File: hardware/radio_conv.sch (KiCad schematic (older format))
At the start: 15 parts

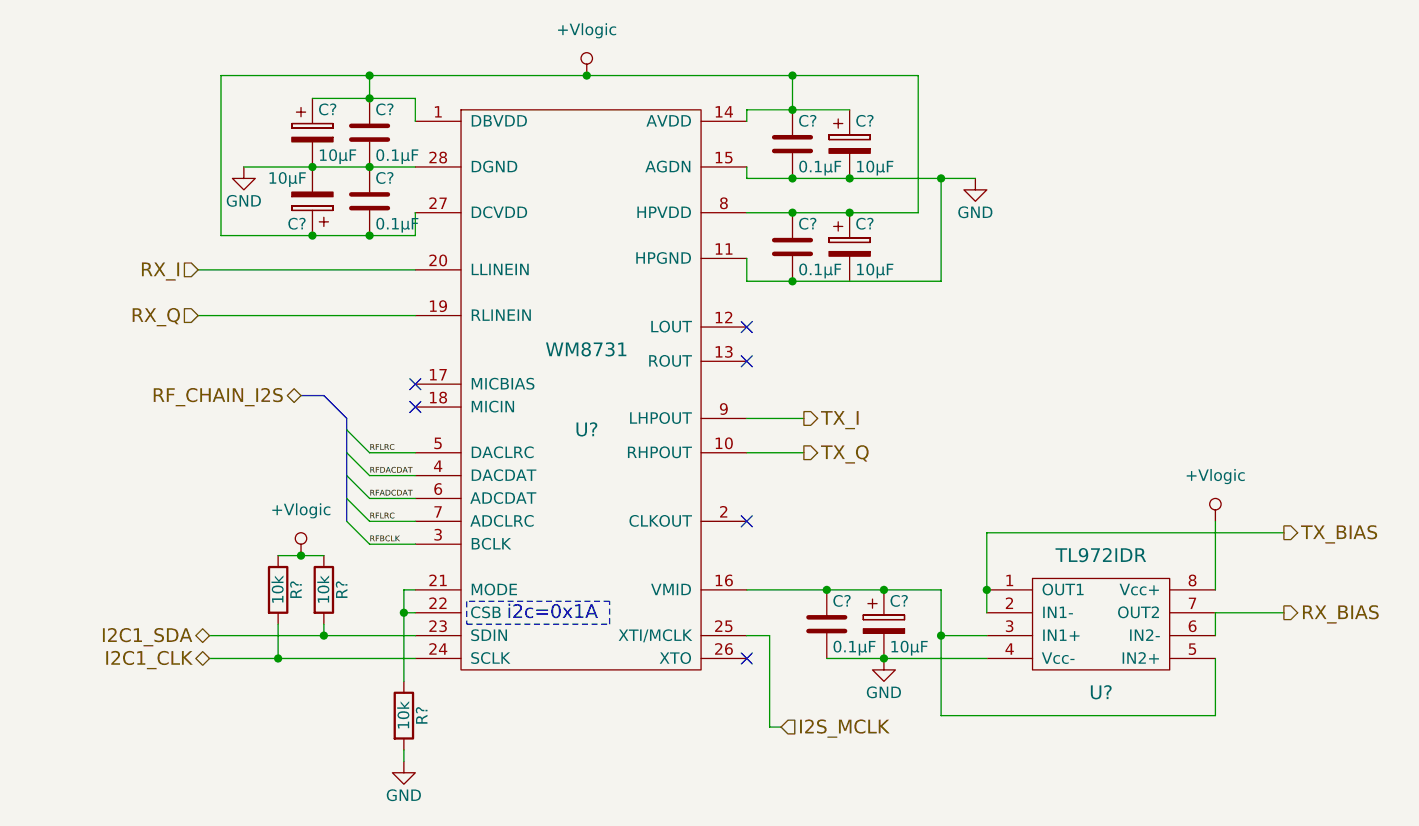
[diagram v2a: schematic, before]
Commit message: Allocated CPU some pins and made minor adjustments here and there
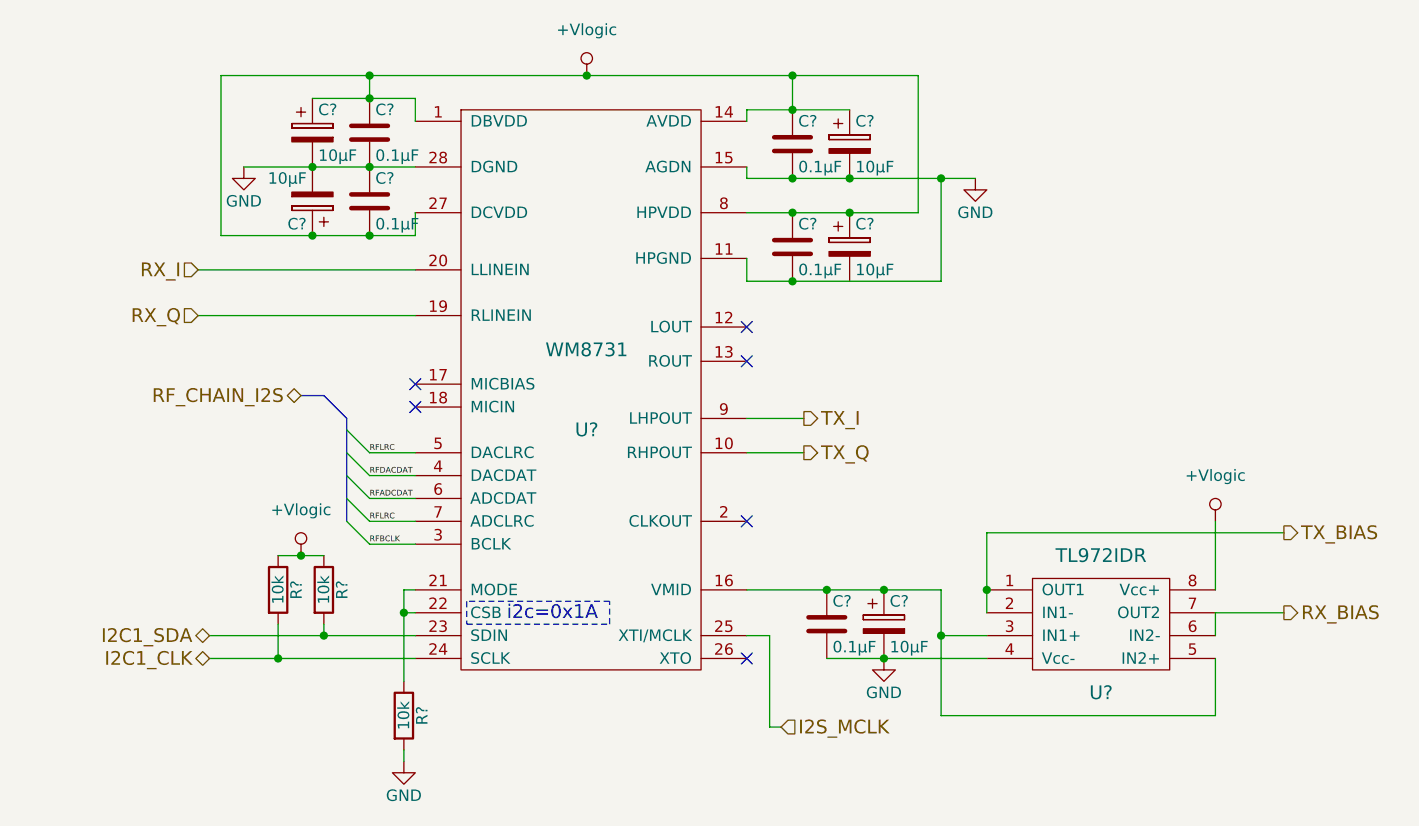
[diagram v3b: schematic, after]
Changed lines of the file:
@@
 $EndComp
 Wire Wire Line
-	4300 2600 4600 2600
-Wire Wire Line
-	4600 2600 4850 2600
-Wire Wire Line
-	4850 2600 5050 2600
+	4300 2600 5050 2600
 Wire Wire Line
 	5050 2300 5050 2400
 Wire Wire Line
-	4600 2300 4850 2300
-Wire Wire Line
-	4850 2300 5050 2300
+	4600 2300 5050 2300
 Connection ~ 4850 2300
 Wire Wire Line
 	4850 2300 4850 2200
 Wire Wire Line
-	4200 2200 4850 2200
-Wire Wire Line
-	4850 2200 5800 2200
-Wire Wire Line
-	5800 2200 6700 2200
-Wire Wire Line
-	6700 2200 7250 2200
+	4200 2200 7250 2200
 Connection ~ 4600 2600
 Connection ~ 4850 2600
@@
 Connection ~ 5800 2200
 Wire Wire Line
-	6500 2350 6700 2350
-Wire Wire Line
-	6700 2350 6950 2350
+	6500 2350 6950 2350
 Wire Wire Line
 	6500 2350 6500 2400
 Connection ~ 6700 2350
 Wire Wire Line
-	6500 2650 6700 2650
-Wire Wire Line
-	6700 2650 6950 2650
-Wire Wire Line
-	6950 2650 7350 2650
-Wire Wire Line
-	7350 2650 7500 2650
+	6500 2650 7500 2650
 Wire Wire Line
 	6500 2650 6500 2600
@@
 	7250 2800 7250 2200
 Wire Wire Line
-	6500 2800 6700 2800
-Wire Wire Line
-	6700 2800 6950 2800
-Wire Wire Line
-	6950 2800 7250 2800
+	6500 2800 7250 2800
 Connection ~ 6700 2200
 Connection ~ 6950 2800
@@
 	6500 3000 6500 3100
 Wire Wire Line
-	6500 3100 6700 3100
-Wire Wire Line
-	6700 3100 7350 3100
+	6500 3100 7350 3100
 Wire Wire Line
 	7350 3100 7350 2650
@@
 NoConn ~ 5050 3650
 Wire Wire Line
-	4200 2900 4600 2900
-Wire Wire Line
-	4600 2900 4850 2900
-Wire Wire Line
-	4850 2900 5050 2900
+	4200 2900 5050 2900
 Wire Wire Line
 	5050 2900 5050 2800
@@
 $EndComp
 Wire Wire Line
-	4150 4650 4650 4650
-Wire Wire Line
-	4650 4650 5050 4650
+	4150 4650 5050 4650
 Wire Wire Line
 	4650 4650 4650 4600
 Wire Wire Line
-	4150 4750 4450 4750
-Wire Wire Line
-	4450 4750 5050 4750
+	4150 4750 5050 4750
 Wire Wire Line
 	4450 4750 4450 4600
@@
 $EndComp
 Wire Wire Line
-	6500 4450 6850 4450
-Wire Wire Line
-	6850 4450 7100 4450
-Wire Wire Line
-	7100 4450 7350 4450
+	6500 4450 7350 4450
 Connection ~ 6850 4450
 Wire Wire Line
-	6850 4750 7100 4750
-Wire Wire Line
-	7100 4750 7550 4750
+	6850 4750 7550 4750
 $Comp
 L GND #PWR043
@@
 	4650 3600 4750 3700
 Wire Bus Line
-	4750 3700 4750 3750
-Wire Bus Line
-	4750 3750 4750 3850
-Wire Bus Line
-	4750 3850 4750 3950
-Wire Bus Line
-	4750 3950 4750 4050
-Wire Bus Line
-	4750 4050 4750 4150
+	4750 3700 4750 4150
 Wire Bus Line
 	4650 3600 4550 3600
@@
 	5050 4550 5000 4550
 Wire Wire Line
-	5000 4450 5000 4550
-Wire Wire Line
-	5000 4550 5000 4850
+	5000 4450 5000 4850
 Text Notes 5450 4590 0    60   ~ 0
 i2c=0x1A
@@
 $EndComp
 Wire Wire Line
-	7350 4450 7350 4650
-Wire Wire Line
-	7350 4650 7350 5000
+	7350 4450 7350 5000
 Wire Wire Line
 	7350 4650 7550 4650
@@
 Connection ~ 7100 4750
 Wire Wire Line
-	7550 4200 7550 4450
-Wire Wire Line
-	7550 4450 7550 4550
+	7550 4200 7550 4550
 Wire Wire Line
 	8550 4550 8550 4650
@@
 Connection ~ 5000 4550
 Wire Wire Line
-	4450 4300 4550 4300
-Wire Wire Line
-	4550 4300 4650 4300
+	4450 4300 4650 4300
 Wire Wire Line
 	5000 4450 5050 4450

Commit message: Fixed 8/11 of issue #4
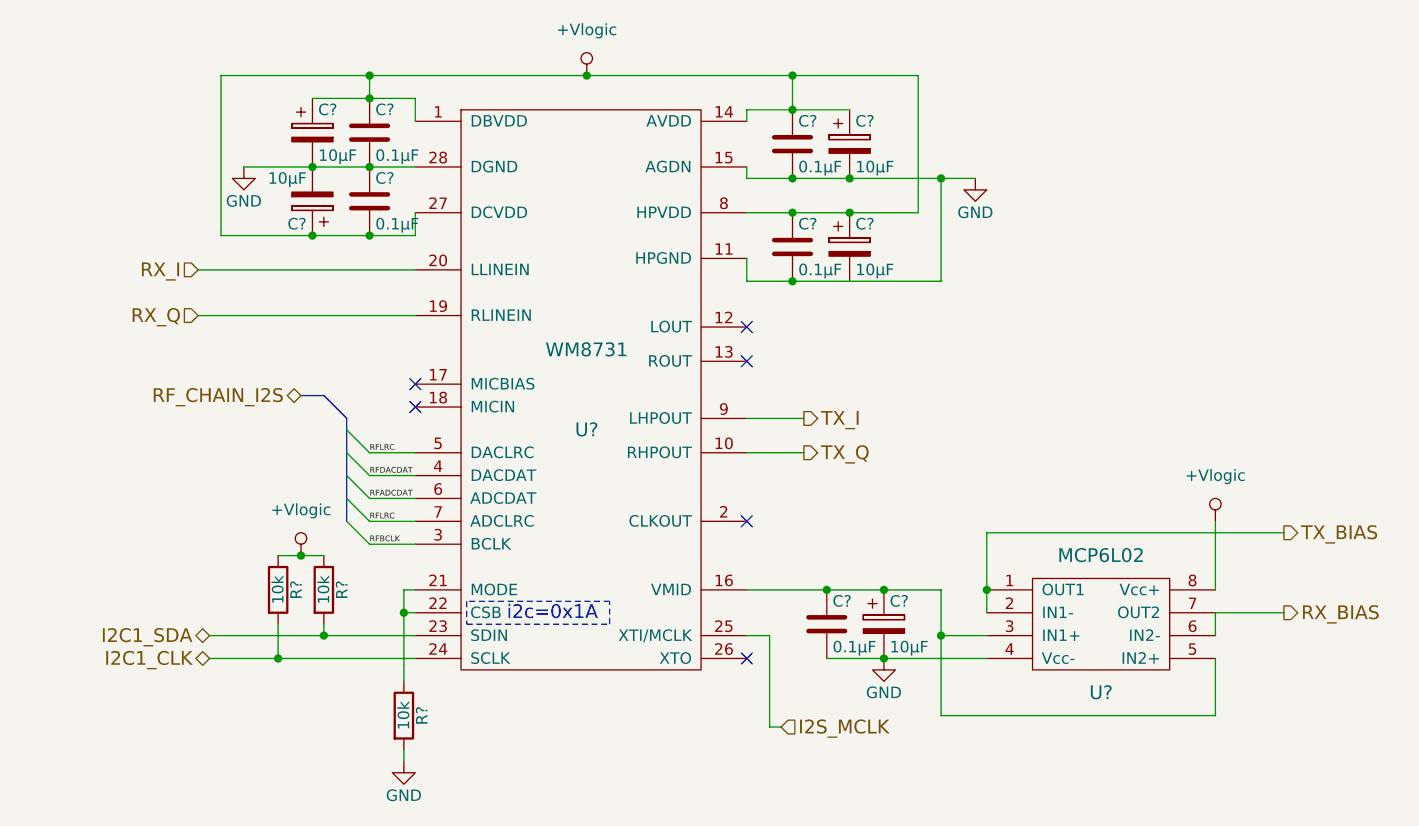
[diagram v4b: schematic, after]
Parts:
- U?: value TL972IDR -> MCP6L02
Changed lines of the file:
@@
-$Comp
-L CP C?
-U 1 1 57E4C126
-P 6950 2500
-F 0 "C?" H 6975 2600 50  0000 L CNN
-F 1 "10µF" H 6975 2400 50  0000 L CNN
-F 2 "" H 6988 2350 50  0000 C CNN
-F 3 "" H 6950 2500 50  0000 C CNN
-	1    6950 2500
-	1    0    0    -1
-$EndComp
-$Comp
-L CP C?
-U 1 1 57E4C12D
-P 6950 2950
-F 0 "C?" H 6975 3050 50  0000 L CNN
-F 1 "10µF" H 6975 2850 50  0000 L CNN
-F 2 "" H 6988 2800 50  0000 C CNN
-F 3 "" H 6950 2950 50  0000 C CNN
-	1    6950 2950
-	1    0    0    -1
-$EndComp
 $Comp
 L CP C?
@@
 $EndComp
 Wire Wire Line
-	7250 2800 7250 2200
-Wire Wire Line
-	6500 2800 7250 2800
+	7250 2200 7250 2800
+Wire Wire Line
+	7250 2800 6500 2800
 Connection ~ 6700 2200
 Connection ~ 6950 2800
@@
 P 8050 4600
 F 0 "U?" H 8050 4300 60  0000 C CNN
-F 1 "TL972IDR" H 8050 4900 60  0000 C CNN
+F 1 "MCP6L02" H 8050 4900 60  0000 C CNN
 F 2 "" H 8100 4600 60  0001 C CNN
 F 3 "" H 8100 4600 60  0001 C CNN
@@
 Wire Wire Line
 	5000 5200 5000 5150
+$Comp
+L CP C?
+U 1 1 57E4C12D
+P 6950 2950
+F 0 "C?" H 6975 3050 50  0000 L CNN
+F 1 "10µF" H 6975 2850 50  0000 L CNN
+F 2 "" H 6988 2800 50  0000 C CNN
+F 3 "" H 6950 2950 50  0000 C CNN
+	1    6950 2950
+	1    0    0    -1
+$EndComp
+$Comp
+L CP C?
+U 1 1 57E4C126
+P 6950 2500
+F 0 "C?" H 6975 2600 50  0000 L CNN
+F 1 "10µF" H 6975 2400 50  0000 L CNN
+F 2 "" H 6988 2350 50  0000 C CNN
+F 3 "" H 6950 2500 50  0000 C CNN
+	1    6950 2500
+	1    0    0    -1
+$EndComp
 $EndSCHEMATC

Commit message: Added annotation so willing prove readers can reference components more easily
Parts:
- gave numbers to parts that had none: 15
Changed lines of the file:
@@
 $EndDescr
 $Comp
-L WM8731 U?
+L WM8731 U701
 U 1 1 57E4C10B
 P 5800 3600
-F 0 "U?" H 5800 3450 60  0000 C CNN
+F 0 "U701" H 5800 3450 60  0000 C CNN
 F 1 "WM8731" H 5800 3800 60  0000 C CNN
 F 2 "" H 5800 4050 60  0001 C CNN
@@
 $EndComp
 $Comp
-L +Vlogic #PWR039
+L +Vlogic #PWR704
 U 1 1 57E4C112
 P 5800 2200
-F 0 "#PWR039" H 5800 2000 50  0001 C CNN
+F 0 "#PWR704" H 5800 2000 50  0001 C CNN
 F 1 "+Vlogic" H 5800 2400 50  0000 C CNN
 F 2 "" H 5800 2200 50  0000 C CNN
@@
 $EndComp
 $Comp
-L CP C?
+L CP C701
 U 1 1 57E4C118
 P 4600 2450
-F 0 "C?" H 4625 2550 50  0000 L CNN
+F 0 "C701" H 4625 2550 50  0000 L CNN
 F 1 "10µF" H 4625 2350 50  0000 L CNN
 F 2 "" H 4638 2300 50  0000 C CNN
@@
 $EndComp
 $Comp
-L CP C?
+L CP C702
 U 1 1 57E4C11F
 P 4600 2750
-F 0 "C?" H 4625 2850 50  0000 L CNN
+F 0 "C702" H 4625 2850 50  0000 L CNN
 F 1 "10µF" H 4625 2650 50  0000 L CNN
 F 2 "" H 4638 2600 50  0000 C CNN
@@
 $EndComp
 $Comp
-L CP C?
+L CP C710
 U 1 1 57E4C134
 P 7100 4600
-F 0 "C?" H 7125 4700 50  0000 L CNN
+F 0 "C710" H 7125 4700 50  0000 L CNN
 F 1 "10µF" H 7125 4500 50  0000 L CNN
 F 2 "" H 7138 4450 50  0000 C CNN
@@
 $EndComp
 $Comp
-L C C?
+L C C703
 U 1 1 57E4C13B
 P 4850 2450
-F 0 "C?" H 4875 2550 50  0000 L CNN
+F 0 "C703" H 4875 2550 50  0000 L CNN
 F 1 "0.1µF" H 4875 2350 50  0000 L CNN
 F 2 "" H 4888 2300 50  0000 C CNN
@@
 $EndComp
 $Comp
-L C C?
+L C C704
 U 1 1 57E4C142
 P 4850 2750
-F 0 "C?" H 4875 2850 50  0000 L CNN
+F 0 "C704" H 4875 2850 50  0000 L CNN
 F 1 "0.1µF" H 4875 2650 50  0000 L CNN
 F 2 "" H 4888 2600 50  0000 C CNN
@@
 $EndComp
 $Comp
-L GND #PWR040
+L GND #PWR701
 U 1 1 57E4C149
 P 4300 2600
-F 0 "#PWR040" H 4300 2350 50  0001 C CNN
+F 0 "#PWR701" H 4300 2350 50  0001 C CNN
 F 1 "GND" H 4300 2450 50  0000 C CNN
 F 2 "" H 4300 2600 50  0000 C CNN
@@
 Connection ~ 4850 2600
 $Comp
-L C C?
+L C C705
 U 1 1 57E4C15D
 P 6700 2500
-F 0 "C?" H 6725 2600 50  0000 L CNN
+F 0 "C705" H 6725 2600 50  0000 L CNN
 F 1 "0.1µF" H 6725 2400 50  0000 L CNN
 F 2 "" H 6738 2350 50  0000 C CNN
@@
 $EndComp
 $Comp
-L C C?
+L C C706
 U 1 1 57E4C164
 P 6700 2950
-F 0 "C?" H 6725 3050 50  0000 L CNN
+F 0 "C706" H 6725 3050 50  0000 L CNN
 F 1 "0.1µF" H 6725 2850 50  0000 L CNN
 F 2 "" H 6738 2800 50  0000 C CNN
@@
 Connection ~ 6950 2650
 $Comp
-L GND #PWR041
+L GND #PWR706
 U 1 1 57E4C178
 P 7500 2650
-F 0 "#PWR041" H 7500 2400 50  0001 C CNN
+F 0 "#PWR706" H 7500 2400 50  0001 C CNN
 F 1 "GND" H 7500 2500 50  0000 C CNN
 F 2 "" H 7500 2650 50  0000 C CNN
@@
 Connection ~ 4600 2900
 $Comp
-L +Vlogic #PWR042
+L +Vlogic #PWR702
 U 1 1 57E4C199
 P 4550 4300
-F 0 "#PWR042" H 4550 4100 50  0001 C CNN
+F 0 "#PWR702" H 4550 4100 50  0001 C CNN
 F 1 "+Vlogic" H 4550 4500 50  0000 C CNN
 F 2 "" H 4550 4300 50  0000 C CNN
@@
 $EndComp
 $Comp
-L R R?
+L R R701
 U 1 1 57E4C19F
 P 4450 4450
-F 0 "R?" V 4530 4450 50  0000 C CNN
+F 0 "R701" V 4530 4450 50  0000 C CNN
 F 1 "10k" V 4450 4450 50  0000 C CNN
 F 2 "" V 4380 4450 50  0000 C CNN
@@
 $EndComp
 $Comp
-L R R?
+L R R702
 U 1 1 57E4C1A6
 P 4650 4450
-F 0 "R?" V 4730 4450 50  0000 C CNN
+F 0 "R702" V 4730 4450 50  0000 C CNN
 F 1 "10k" V 4650 4450 50  0000 C CNN
 F 2 "" V 4580 4450 50  0000 C CNN
@@
 Connection ~ 4550 4300
 $Comp
-L C C?
+L C C707
 U 1 1 57E4C1B6
 P 6850 4600
-F 0 "C?" H 6875 4700 50  0000 L CNN
+F 0 "C707" H 6875 4700 50  0000 L CNN
 F 1 "0.1µF" H 6875 4500 50  0000 L CNN
 F 2 "" H 6888 4450 50  0000 C CNN
@@
 	6850 4750 7550 4750
 $Comp
-L GND #PWR043
+L GND #PWR705
 U 1 1 57E4C1C1
 P 7100 4750
-F 0 "#PWR043" H 7100 4500 50  0001 C CNN
+F 0 "#PWR705" H 7100 4500 50  0001 C CNN
 F 1 "GND" H 7100 4600 50  0000 C CNN
 F 2 "" H 7100 4750 50  0000 C CNN
@@
 RX_Q
 $Comp
-L GND #PWR044
+L GND #PWR703
 U 1 1 57E4C1DF
 P 5000 5200
-F 0 "#PWR044" H 5000 4950 50  0001 C CNN
+F 0 "#PWR703" H 5000 4950 50  0001 C CNN
 F 1 "GND" H 5000 5050 50  0000 C CNN
 F 2 "" H 5000 5200 50  0000 C CNN
@@
 	6500 3850 6750 3850
 $Comp
-L TL972IDR U?
+L TL972IDR U702
 U 1 1 57E46913
 P 8050 4600
-F 0 "U?" H 8050 4300 60  0000 C CNN
+F 0 "U702" H 8050 4300 60  0000 C CNN
 F 1 "MCP6L02" H 8050 4900 60  0000 C CNN
 F 2 "" H 8100 4600 60  0001 C CNN
@@
 	8550 4550 8550 4650
 $Comp
-L +Vlogic #PWR?
+L +Vlogic #PWR707
 U 1 1 57E46B0D
 P 8550 4150
-F 0 "#PWR?" H 8550 3950 50  0001 C CNN
+F 0 "#PWR707" H 8550 3950 50  0001 C CNN
 F 1 "+Vlogic" H 8550 4350 50  0000 C CNN
 F 2 "" H 8550 4150 50  0000 C CNN
@@
 RFBCLK
 $Comp
-L R R?
+L R R703
 U 1 1 57E786C6
 P 5000 5000
-F 0 "R?" V 5080 5000 50  0000 C CNN
+F 0 "R703" V 5080 5000 50  0000 C CNN
 F 1 "10k" V 5000 5000 50  0000 C CNN
 F 2 "" V 4930 5000 50  0000 C CNN
@@
 	5000 5200 5000 5150
 $Comp
-L CP C?
+L CP C709
 U 1 1 57E4C12D
 P 6950 2950
-F 0 "C?" H 6975 3050 50  0000 L CNN
+F 0 "C709" H 6975 3050 50  0000 L CNN
 F 1 "10µF" H 6975 2850 50  0000 L CNN
 F 2 "" H 6988 2800 50  0000 C CNN
@@
 $EndComp
 $Comp
-L CP C?
+L CP C708
 U 1 1 57E4C126
 P 6950 2500
-F 0 "C?" H 6975 2600 50  0000 L CNN
+F 0 "C708" H 6975 2600 50  0000 L CNN
 F 1 "10µF" H 6975 2400 50  0000 L CNN
 F 2 "" H 6988 2350 50  0000 C CNN

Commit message: fixed some more ERC errors
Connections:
- net GND: now also C709.2
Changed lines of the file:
@@
 $EndComp
 $Comp
-L +Vlogic #PWR041
+L +Vlogic #PWR046
 U 1 1 57E4C112
 P 5800 2200
-F 0 "#PWR041" H 5800 2000 50  0001 C CNN
+F 0 "#PWR046" H 5800 2000 50  0001 C CNN
 F 1 "+Vlogic" H 5800 2400 50  0000 C CNN
 F 2 "" H 5800 2200 50  0000 C CNN
@@
 $EndComp
 $Comp
-L GND #PWR042
+L GND #PWR047
 U 1 1 57E4C149
 P 4300 2600
-F 0 "#PWR042" H 4300 2350 50  0001 C CNN
+F 0 "#PWR047" H 4300 2350 50  0001 C CNN
 F 1 "GND" H 4300 2450 50  0000 C CNN
 F 2 "" H 4300 2600 50  0000 C CNN
@@
 Connection ~ 6950 2650
 $Comp
-L GND #PWR043
+L GND #PWR048
 U 1 1 57E4C178
 P 7500 2650
-F 0 "#PWR043" H 7500 2400 50  0001 C CNN
+F 0 "#PWR048" H 7500 2400 50  0001 C CNN
 F 1 "GND" H 7500 2500 50  0000 C CNN
 F 2 "" H 7500 2650 50  0000 C CNN
@@
 Connection ~ 4600 2900
 $Comp
-L +Vlogic #PWR044
+L +Vlogic #PWR049
 U 1 1 57E4C199
 P 4550 4300
-F 0 "#PWR044" H 4550 4100 50  0001 C CNN
+F 0 "#PWR049" H 4550 4100 50  0001 C CNN
 F 1 "+Vlogic" H 4550 4500 50  0000 C CNN
 F 2 "" H 4550 4300 50  0000 C CNN
@@
 	6850 4750 7550 4750
 $Comp
-L GND #PWR045
+L GND #PWR050
 U 1 1 57E4C1C1
 P 7100 4750
-F 0 "#PWR045" H 7100 4500 50  0001 C CNN
+F 0 "#PWR050" H 7100 4500 50  0001 C CNN
 F 1 "GND" H 7100 4600 50  0000 C CNN
 F 2 "" H 7100 4750 50  0000 C CNN
@@
 RX_Q
 $Comp
-L GND #PWR046
+L GND #PWR051
 U 1 1 57E4C1DF
 P 5000 5200
-F 0 "#PWR046" H 5000 4950 50  0001 C CNN
+F 0 "#PWR051" H 5000 4950 50  0001 C CNN
 F 1 "GND" H 5000 5050 50  0000 C CNN
 F 2 "" H 5000 5200 50  0000 C CNN
@@
 	8550 4550 8550 4650
 $Comp
-L +Vlogic #PWR047
+L +Vlogic #PWR052
 U 1 1 57E46B0D
 P 8550 4150
-F 0 "#PWR047" H 8550 3950 50  0001 C CNN
+F 0 "#PWR052" H 8550 3950 50  0001 C CNN
 F 1 "+Vlogic" H 8550 4350 50  0000 C CNN
 F 2 "" H 8550 4150 50  0000 C CNN
@@
 	1    0    0    -1
 $EndComp
+Connection ~ 6950 3100
+Connection ~ 5050 4250
+Connection ~ 5050 4050
+Connection ~ 5050 3950
 $EndSCHEMATC
